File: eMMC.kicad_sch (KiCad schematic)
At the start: 0 parts

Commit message: PMIC DCDC
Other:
- title: Leaf RV1126 Power -> Leaf RV1126 PMIC RK809
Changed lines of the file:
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@@
   (paper "A4")
   (title_block
-    (title "Leaf RV1126 Power")
+    (title "Leaf RV1126 PMIC RK809")
     (date "2023-02-23")
     (rev "1")

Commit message: updated: PMIC codec
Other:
- title: Leaf RV1126 PMIC RK809 -> Leaf RV1126 PMIC RK809 Codec
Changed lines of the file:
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@@
   (paper "A4")
   (title_block
-    (title "Leaf RV1126 PMIC RK809")
-    (date "2023-02-23")
+    (title "Leaf RV1126 PMIC RK809 Codec")
+    (date "2023-02-25")
     (rev "1")
     (company "Qingdao IotPi Information Technology")

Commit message: updated: titles
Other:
- title: Leaf RV1126 PMIC RK809 Codec -> Leaf RV1126 RK809 eMMC
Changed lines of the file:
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@@
   (paper "A4")
   (title_block
-    (title "Leaf RV1126 PMIC RK809 Codec")
+    (title "Leaf RV1126 RK809 eMMC")
     (date "2023-02-25")
     (rev "1")

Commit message: Updated eMMC
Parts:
- added C57: 100nF X5R 6.3V, Capacitor_SMD:C_0201_0603Metric, symbol Device:C
- added R40 (x2): 4.7K 5%, Resistor_SMD:R_0402_1005Metric, symbol Device:R
- added R40 (x2): 0R 5%, Resistor_SMD:R_0402_1005Metric, symbol Device:R
- added U1: rv1126/rv1109, symbol CPU_Rockchip:rv1126_rv1109
- added U5: MTFC4GACAJCN, symbol Memory_eMMC:MTFC4GACAJCN
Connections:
- new net EMMC_CLK: U1.T1 (FLASH_CLE/EMMC_CLKO/GPIO0_D7_d), U5.M6 (CLK)
- new net EMMC_CMD: U1.T4 (FLASH_WRn/EMMC_CMD/GPIO0_D5_u), U5.M5 (CMD)
- new net EMMC_D0: U1.W2 (FLASH_D0/EMMC_D0/GPIO0_C4_u), U5.A3 (DATA0)
- new net EMMC_D1: U1.W1 (FLASH_D1/EMMC_D1/GPIO0_C5_u), U5.A4 (DATA1)
- new net EMMC_D2: U1.V4 (FLASH_D2/EMMC_D2/GPIO0_C6_u), U5.A5 (DATA2)
- new net EMMC_D3: U1.V3 (FLASH_D3/EMMC_D3/GPIO0_C7_u), U5.B2 (DATA3)
- new net EMMC_D4: U1.V2 (FLASH_D4/EMMC_D4/GPIO0_D0_u), U5.B3 (DATA4)
- new net EMMC_D5: U1.V1 (FLASH_D5/EMMC_D5/FSPI_CS1n/GPIO0_D1_u), U5.B4 (DATA5)
- new net EMMC_D6: U1.U4 (FLASH_D6/EMMC_D6/GPIO0_D2_u), U5.B5 (DATA6)
- new net EMMC_D7: U1.U3 (FLASH_D7/EMMC_D7/GPIO0_D3_u), U5.B6 (DATA7)
- new net EMMC_~{RST}: U1.R3 (FLASH_WPn/EMMC_RSTn/FSPI_CLK/GPIO1_A3_d), U5.K5 (~{RST})
- new net FLASH_VOL_SEL: R40.2
- new net GND: C57.2, R40.1
- new net VCC3V3_SYS: R40.2
- new net VCCIO_FLASH: C57.1, R40.2, R40.2, U1.P6 (VCCIO1_VDD)
- new net VCC_1V8: R40.1
- new net VCC_3V3: R40.1
- no-connect marks 0 -> 5
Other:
- note added: "DNP"

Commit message: Updated eMMC
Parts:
- added C57 (x2): 4.7Vf X5R 6.3V, Capacitor_SMD:C_0402_1005Metric, symbol Device:C
- added C57 (x3): 100nF X5R 16V, Capacitor_SMD:C_0402_1005Metric, symbol Device:C
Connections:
- net GND: now also C57.2, C57.2, C57.2, C57.2, C57.2
- net VCCIO_FLASH: now also U5.C6 (V_{CCQ}), U5.M4 (V_{CCQ}), U5.N4 (V_{CCQ}), U5.P3 (V_{CCQ}), U5.P5 (V_{CCQ}), C57.1, C57.1, C57.1
- net VCC_3V3: now also U5.E6 (V_{CC}), U5.F5 (V_{CC}), U5.J10 (V_{CC}), U5.K9 (V_{CC}), C57.1, C57.1
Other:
- moved on the sheet: C57, R40, U1F, U5A

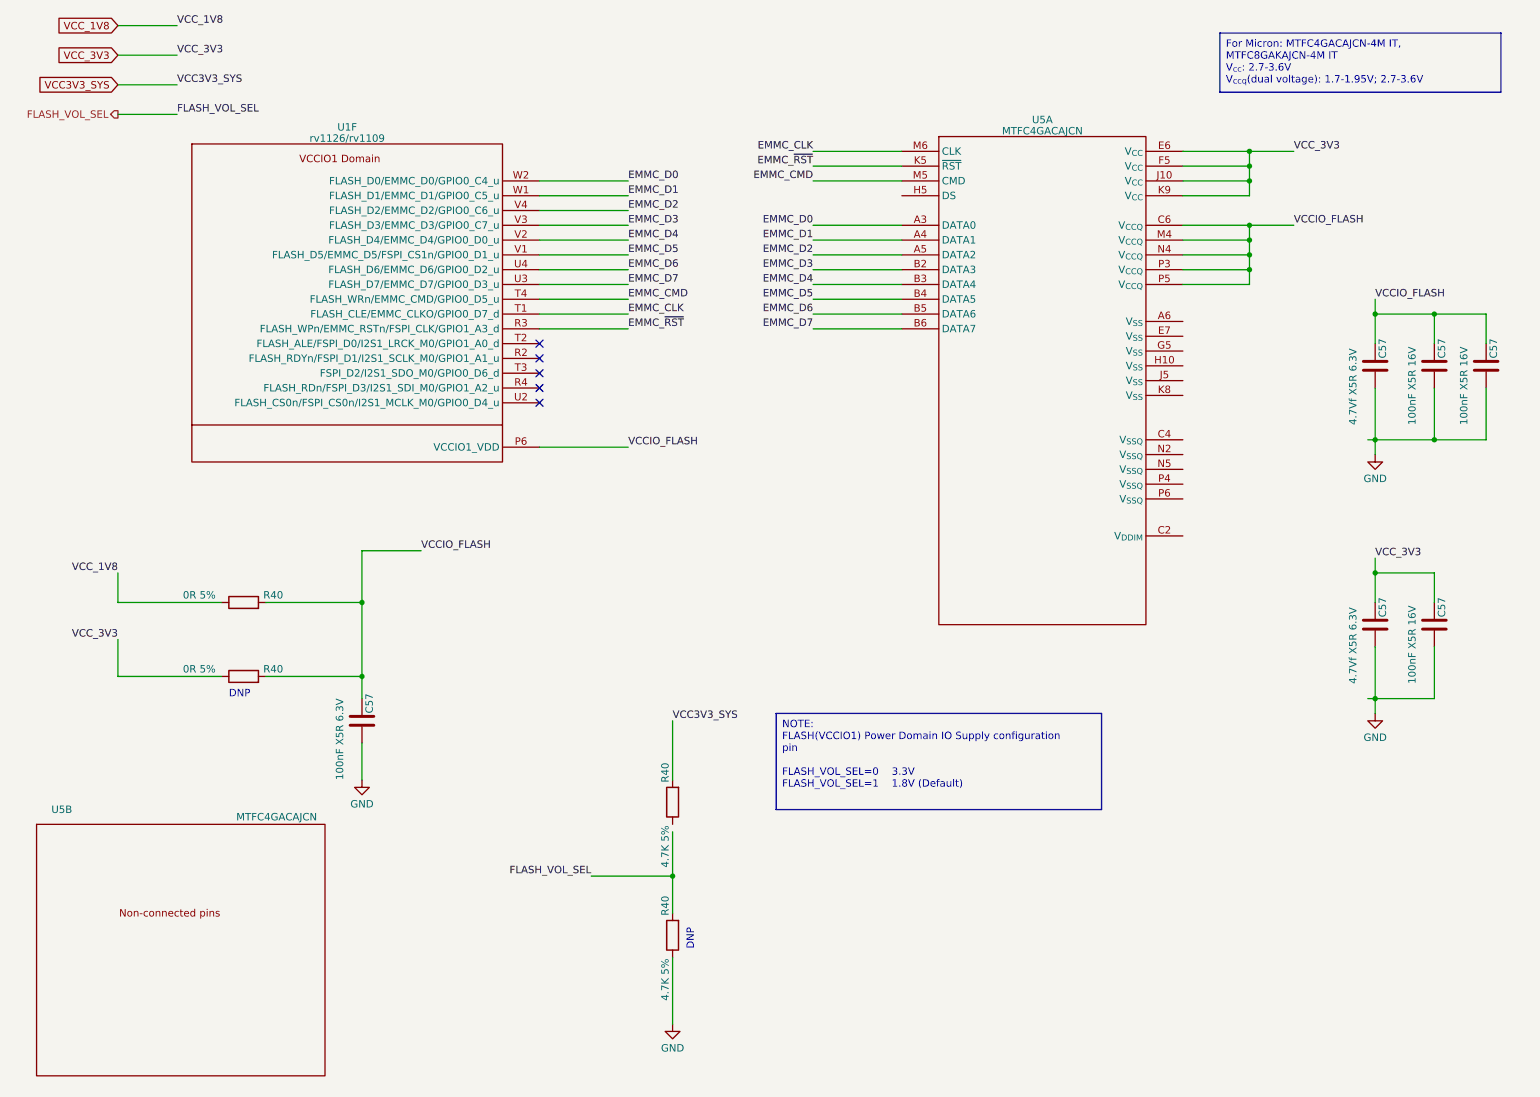
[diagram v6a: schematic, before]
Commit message: link FLASH_VOL_SEL
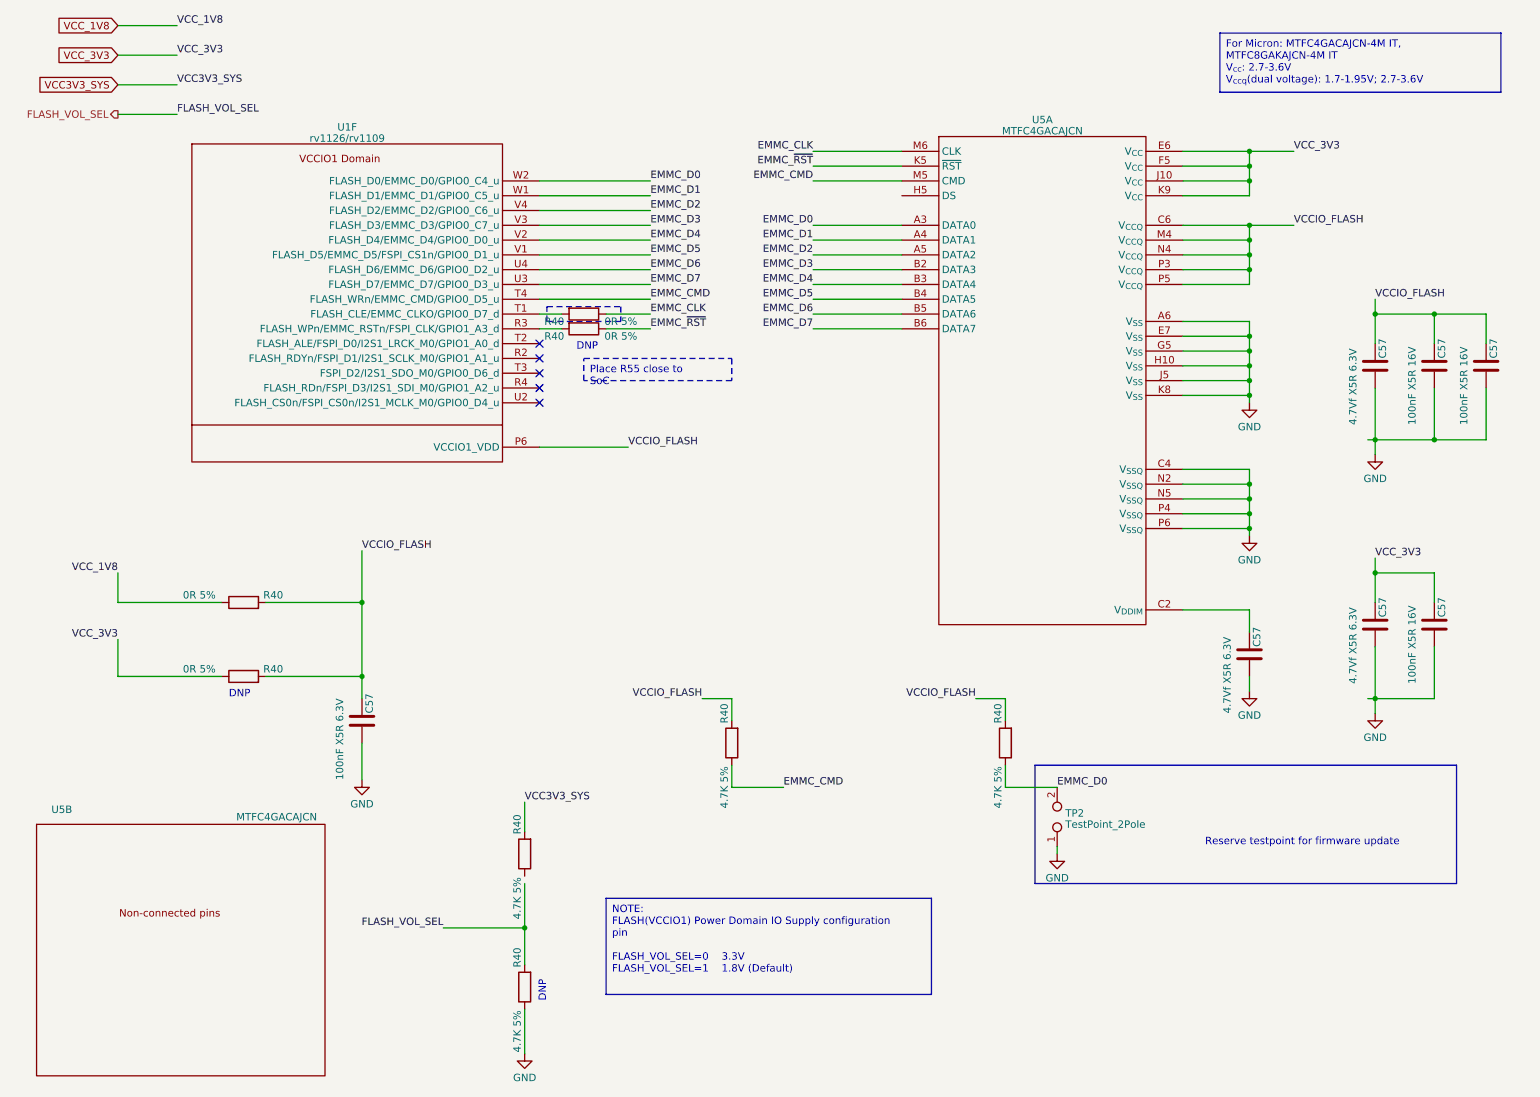
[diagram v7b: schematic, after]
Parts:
- added C57: 4.7Vf X5R 6.3V, Capacitor_SMD:C_0402_1005Metric, symbol Device:C
- added R40 (x2): 0R 5%, Resistor_SMD:R_0402_1005Metric, symbol Device:R
- added R40 (x2): 4.7K 5%, Resistor_SMD:R_0402_1005Metric, symbol Device:R
- added TP2: TestPoint_2Pole, symbol Connector:TestPoint_2Pole
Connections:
- net EMMC_CLK: now also R40.1; no longer U1.T1 (FLASH_CLE/EMMC_CLKO/GPIO0_D7_d)
- net EMMC_CMD: now also R40.1
- net EMMC_D0: now also R40.1, TP2.2
- net EMMC_~{RST}: now also R40.1; no longer U1.R3 (FLASH_WPn/EMMC_RSTn/FSPI_CLK/GPIO1_A3_d)
- net GND: now also U5.A6 (V_{SS}), U5.C4 (V_{SSQ}), U5.E7 (V_{SS}), U5.G5 (V_{SS}), U5.H10 (V_{SS}), U5.J5 (V_{SS}), U5.K8 (V_{SS}), U5.N2 (V_{SSQ}), U5.N5 (V_{SSQ}), U5.P4 (V_{SSQ}), U5.P6 (V_{SSQ}), C57.2, TP2.1
- net VCCIO_FLASH: now also R40.2, R40.2
- net at U5.C2 (V_{DDIM}): now also C57.1
- new net: R40.2, U1.R3 (FLASH_WPn/EMMC_RSTn/FSPI_CLK/GPIO1_A3_d)
- new net: R40.2, U1.T1 (FLASH_CLE/EMMC_CLKO/GPIO0_D7_d)
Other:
- note added: "Reserve testpoint for firmware update"
- moved on the sheet: R40
